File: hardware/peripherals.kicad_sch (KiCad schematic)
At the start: 32 parts, among them J6 Conn_01x02, J7 USB_C_Receptacle_USB2.0_14P, J8 Conn_01x03, Q4 2N7002, SW1 SW_Push, U3 74AHCT1G125, U4 DS3231MZ, U5 USBLC6-2SC6, U6 74AHCT1G32

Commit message: Right-angle button (Alps SKRTLAE010), adjust connector Y positions, add 3D models
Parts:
- SW1: footprint Button_Switch_SMD:SW_Push_1TS009xxxx-xxxx-xxxx_6x6x5mm -> Button_Switch_SMD:SW_Push_1P1T-MP_NO_Horizontal_Alps_SKRTLAE010
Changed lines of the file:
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@@
 			)
 		)
-		(property "Footprint" "Button_Switch_SMD:SW_Push_1TS009xxxx-xxxx-xxxx_6x6x5mm"
+		(property "Footprint" "Button_Switch_SMD:SW_Push_1P1T-MP_NO_Horizontal_Alps_SKRTLAE010"
 			(at 246.38 40.64 0)
 			(hide yes)

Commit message: Replace reverse-mount LED with standard 5050 SK6812 for light pipe
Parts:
- D1: footprint LED_SMD:LED_SK6812MINI-E_3.2x2.8mm_P1.5mm_ReverseMount -> LED_SMD:LED_SK6812_PLCC4_5.0x5.0mm_P3.2mm
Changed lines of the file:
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@@
 			)
 		)
-		(property "Footprint" "LED_SMD:LED_SK6812MINI-E_3.2x2.8mm_P1.5mm_ReverseMount"
+		(property "Footprint" "LED_SMD:LED_SK6812_PLCC4_5.0x5.0mm_P3.2mm"
 			(at 128.27 46.99 0)
 			(hide yes)

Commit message: Fix ERC: update SK6812 symbol to match library
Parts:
- D1: footprint LED_SMD:LED_SK6812_PLCC4_5.0x5.0mm_P3.2mm -> LED_SMD:LED_SK6812MINI-E_3.2x2.8mm_P1.5mm_ReverseMount
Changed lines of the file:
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@@
 			)
 		)
-		(property "Footprint" "LED_SMD:LED_SK6812_PLCC4_5.0x5.0mm_P3.2mm"
+		(property "Footprint" "LED_SMD:LED_SK6812MINI-E_3.2x2.8mm_P1.5mm_ReverseMount"
 			(at 128.27 46.99 0)
 			(hide yes)

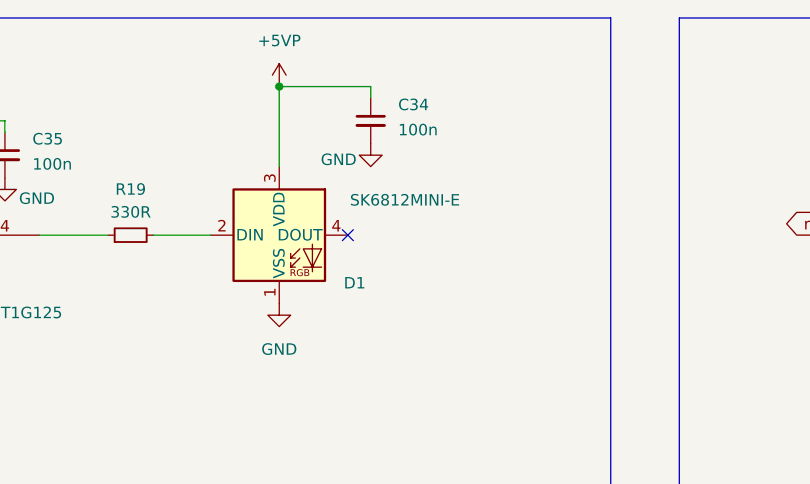
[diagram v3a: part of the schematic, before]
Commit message: Change NeoPixel D1 to WS2812B 5mm SMD (PLCC4)
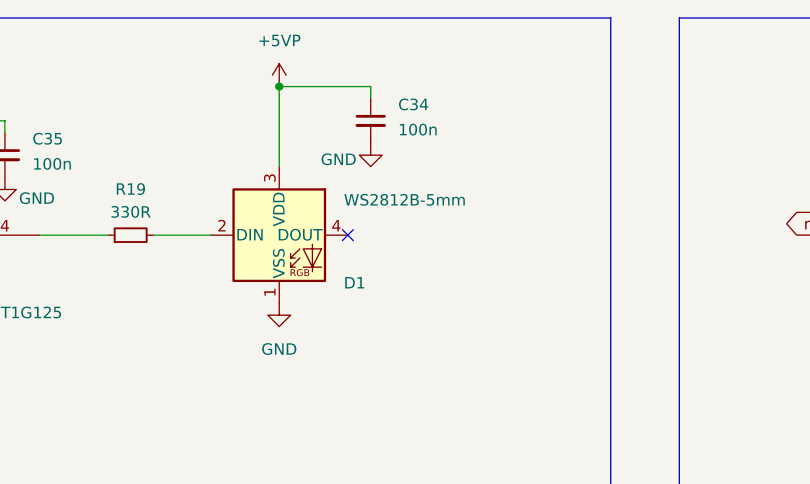
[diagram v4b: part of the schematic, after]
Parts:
- D1: value SK6812MINI-E -> WS2812B-5mm; footprint LED_SMD:LED_SK6812MINI-E_3.2x2.8mm_P1.5mm_ReverseMount -> LED_SMD:LED_WS2812B_PLCC4_5.0x5.0mm_P3.2mm
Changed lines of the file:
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@@
 			)
 		)
-		(property "Value" "SK6812MINI-E"
+		(property "Value" "WS2812B-5mm"
 			(at 140.97 35.4898 0)
 			(show_name no)
@@
 			)
 		)
-		(property "Footprint" "LED_SMD:LED_SK6812MINI-E_3.2x2.8mm_P1.5mm_ReverseMount"
+		(property "Footprint" "LED_SMD:LED_WS2812B_PLCC4_5.0x5.0mm_P3.2mm"
 			(at 128.27 46.99 0)
 			(hide yes)

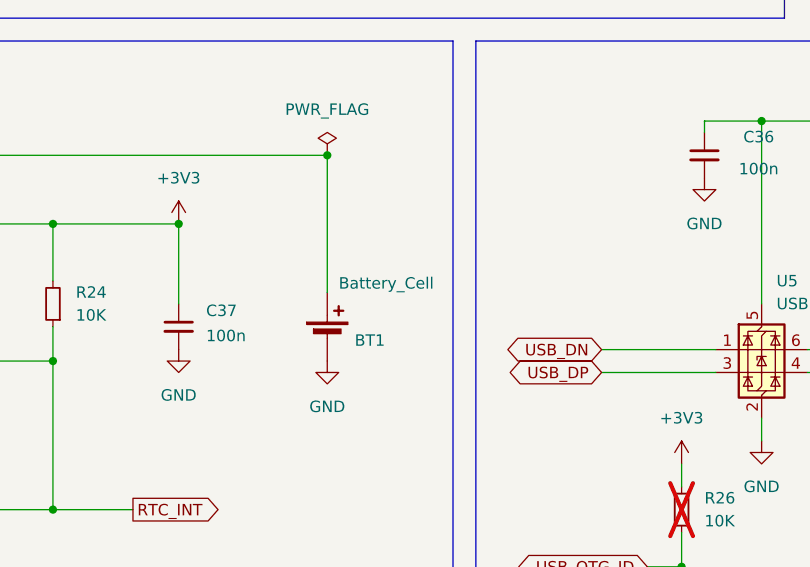
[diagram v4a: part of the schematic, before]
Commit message: fix: add missing BOM values for F1 (3A), Y1 (25MHz), BT1 (CR2032)
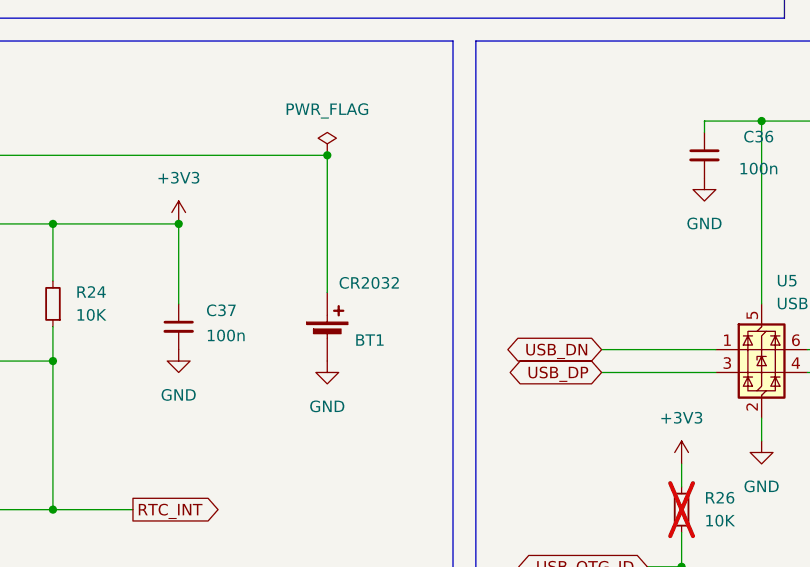
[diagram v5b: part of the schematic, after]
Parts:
- BT1: value Battery_Cell -> CR2032
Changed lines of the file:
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@@
 			)
 		)
-		(property "Value" "Battery_Cell"
+		(property "Value" "CR2032"
 			(at 114.3 99.314 0)
 			(show_name no)

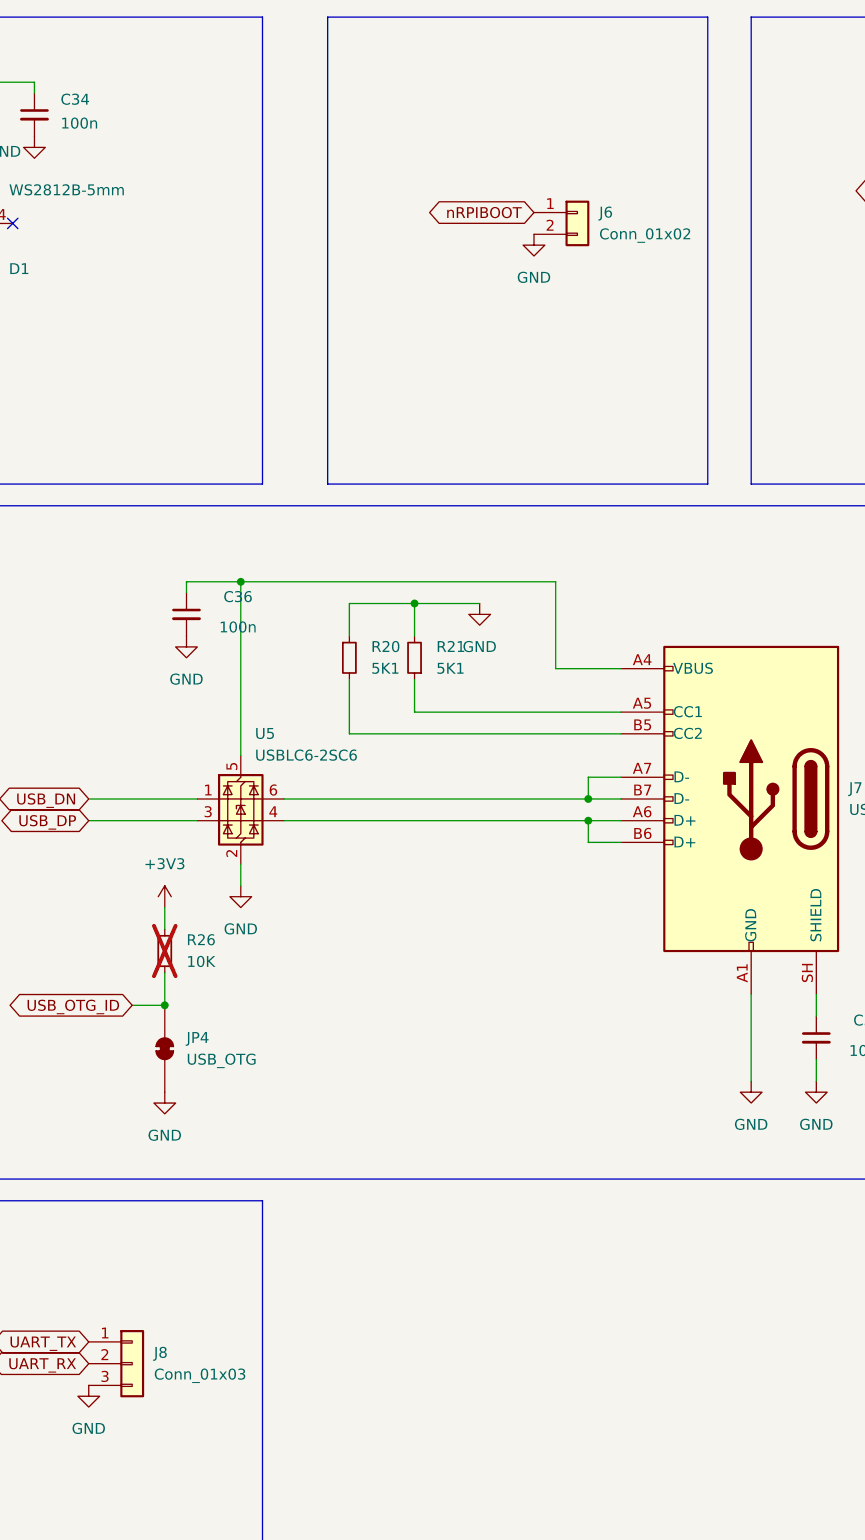
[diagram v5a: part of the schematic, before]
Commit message: feat: replace J6 with PCM12SMTR slide switch, J8 with JST-SH 3-pin
J6 (nRPIBOOT): pin header + jumper → SPDT slide switch (SW_SPDT_312)
J8 (UART debug): 2.54mm pin header → JST-SH SM03B-SRSS-TB (latching)
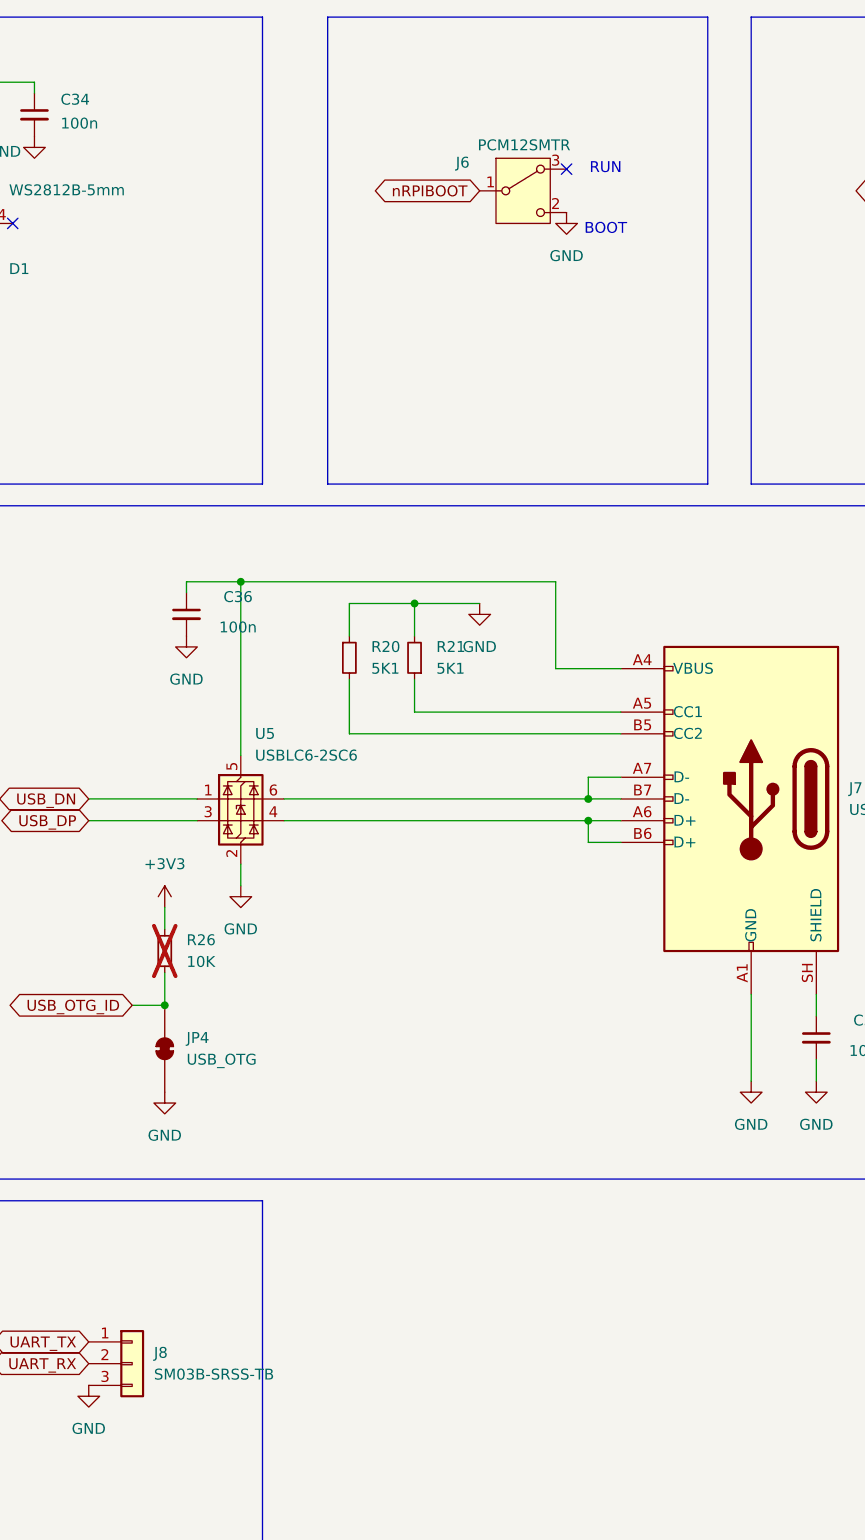
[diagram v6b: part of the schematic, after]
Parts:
- J6: value Conn_01x02 -> PCM12SMTR; footprint Connector_PinHeader_2.54mm:PinHeader_1x02_P2.54mm_Vertical -> Button_Switch_SMD:SW_SPDT_PCM12; symbol Connector_Generic:Conn_01x02 -> Switch:SW_SPDT_312
- J8: value Conn_01x03 -> SM03B-SRSS-TB; footprint Connector_PinHeader_2.54mm:PinHeader_1x03_P2.54mm_Vertical -> Connector_JST:JST_SH_SM03B-SRSS-TB_1x03-1MP_P1.00mm_Horizontal
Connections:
- no-connect marks 2 -> 3
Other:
- note added: "BOOT"
- note added: "RUN"
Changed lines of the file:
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@@
 		)
 	)
+	(text "BOOT"
+		(exclude_from_sim no)
+		(at 203.962 40.132 0)
+		(effects
+			(font
+				(size 1.27 1.27)
+			)
+		)
+	)
+	(text "RUN"
+		(exclude_from_sim no)
+		(at 203.962 33.02 0)
+		(effects
+			(font
+				(size 1.27 1.27)
+			)
+		)
+	)
 	(junction
 		(at 55.88 146.05)
@@
 	)
 	(no_connect
+		(at 199.39 33.02)
+	)
+	(no_connect
 		(at 74.93 100.33)
 	)
@@
 	(global_label "nRPIBOOT"
 		(shape bidirectional)
-		(at 195.58 38.1 180)
+		(at 189.23 35.56 180)
 		(fields_autoplaced yes)
 		(effects
@@
 		)
 		(property "Intersheetrefs" "${INTERSHEET_REFS}"
-			(at 182.2911 38.1 0)
+			(at 175.9411 35.56 0)
 			(hide yes)
 			(show_name no)
@@
 	(symbol
 		(lib_id "power:GND")
-		(at 195.58 40.64 0)
+		(at 199.39 38.1 0)
 		(unit 1)
 		(body_style 1)
@@
 		(fields_autoplaced yes)
 		(property "Reference" "#PWR056"
-			(at 195.58 46.99 0)
+			(at 199.39 44.45 0)
 			(hide yes)
 			(show_name no)
@@
 		)
 		(property "Value" "GND"
-			(at 195.58 45.72 0)
+			(at 199.39 43.18 0)
 			(show_name no)
 			(do_not_autoplace no)
@@
 		)
 		(property "Footprint" ""
-			(at 195.58 40.64 0)
+			(at 199.39 38.1 0)
 			(hide yes)
 			(show_name no)
@@
 		)
 		(property "Datasheet" ""
-			(at 195.58 40.64 0)
+			(at 199.39 38.1 0)
 			(hide yes)
 			(show_name no)
@@
 		)
 		(property "Description" "Power symbol creates a global label with name \"GND\" , ground"
-			(at 195.58 40.64 0)
+			(at 199.39 38.1 0)
 			(hide yes)
 			(show_name no)
@@
 	)
 	(symbol
-		(lib_id "Connector_Generic:Conn_01x02")
-		(at 200.66 38.1 0)
+		(lib_id "Switch:SW_SPDT_312")
+		(at 194.31 35.56 0)
 		(unit 1)
 		(body_style 1)
@@
 		(in_pos_files yes)
 		(dnp no)
-		(fields_autoplaced yes)
 		(property "Reference" "J6"
-			(at 203.2 38.0999 0)
+			(at 186.436 32.258 0)
 			(show_name no)
 			(do_not_autoplace no)
@@
 			)
 		)
-		(property "Value" "Conn_01x02"
-			(at 203.2 40.6399 0)
+		(property "Value" "PCM12SMTR"
+			(at 188.976 30.226 0)
 			(show_name no)
 			(do_not_autoplace no)
@@
 			)
 		)
-		(property "Footprint" "Connector_PinHeader_2.54mm:PinHeader_1x02_P2.54mm_Vertical"
-			(at 200.66 38.1 0)
+		(property "Footprint" "Button_Switch_SMD:SW_SPDT_PCM12"
+			(at 194.31 35.56 0)
 			(hide yes)
 			(show_name no)
@@
 		)
 		(property "Datasheet" ""
-			(at 200.66 38.1 0)
+			(at 194.31 35.56 0)
 			(hide yes)
 			(show_name no)
@@
 			)
 		)
-		(property "Description" "Generic connector, single row, 01x02, script generated (kicad-library-utils/schlib/autogen/connector/)"
-			(at 200.66 38.1 0)
+		(property "Description" "Switch, single pole double throw"
+			(at 194.31 35.56 0)
 			(hide yes)
 			(show_name no)
@@
 		(pin "1"
 		)
+		(pin "3"
+		)
 		(instances
 			(project "granit"
@@
 			)
 		)
-		(property "Value" "Conn_01x03"
+		(property "Value" "SM03B-SRSS-TB"
 			(at 151.13 173.9899 0)
 			(show_name no)
@@
 			)
 		)
-		(property "Footprint" "Connector_PinHeader_2.54mm:PinHeader_1x03_P2.54mm_Vertical"
+		(property "Footprint" "Connector_JST:JST_SH_SM03B-SRSS-TB_1x03-1MP_P1.00mm_Horizontal"
 			(at 148.59 172.72 0)
 			(hide yes)

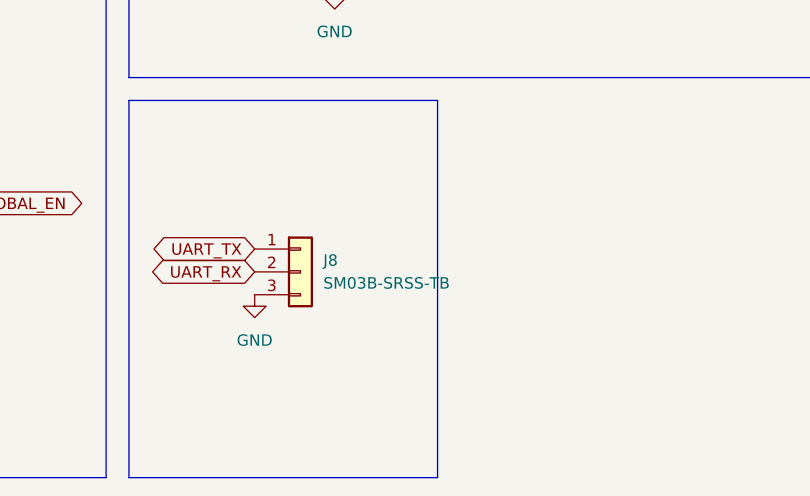
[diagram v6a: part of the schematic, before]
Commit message: fix: J8 use vertical JST-SH (BM03B-SRSS-TB)
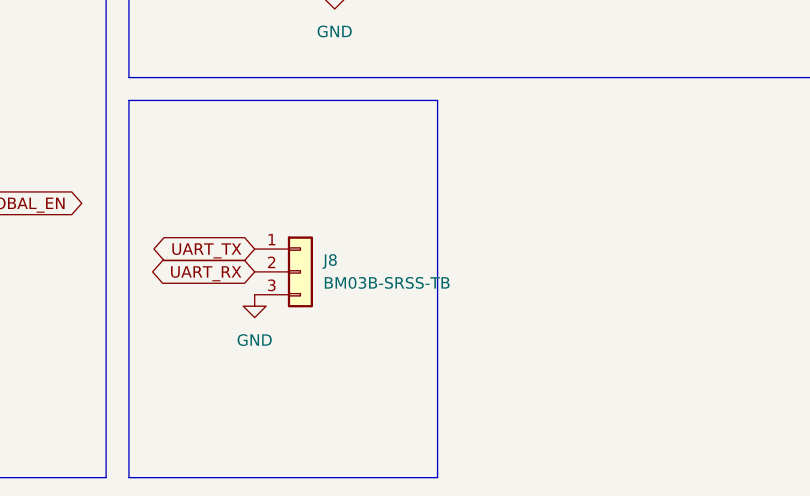
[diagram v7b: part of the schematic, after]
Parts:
- J8: value SM03B-SRSS-TB -> BM03B-SRSS-TB; footprint Connector_JST:JST_SH_SM03B-SRSS-TB_1x03-1MP_P1.00mm_Horizontal -> Connector_JST:JST_SH_BM03B-SRSS-TB_1x03-1MP_P1.00mm_Vertical
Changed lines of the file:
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@@
 			)
 		)
-		(property "Value" "SM03B-SRSS-TB"
+		(property "Value" "BM03B-SRSS-TB"
 			(at 151.13 173.9899 0)
 			(show_name no)
@@
 			)
 		)
-		(property "Footprint" "Connector_JST:JST_SH_SM03B-SRSS-TB_1x03-1MP_P1.00mm_Horizontal"
+		(property "Footprint" "Connector_JST:JST_SH_BM03B-SRSS-TB_1x03-1MP_P1.00mm_Vertical"
 			(at 148.59 172.72 0)
 			(hide yes)

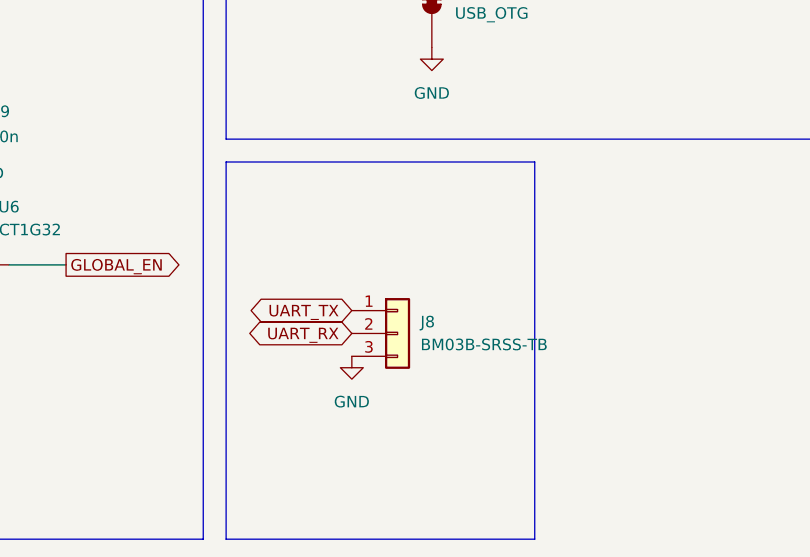
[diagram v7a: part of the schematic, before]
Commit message: fix: J6/J8 wiring and PCB layout after connector swap
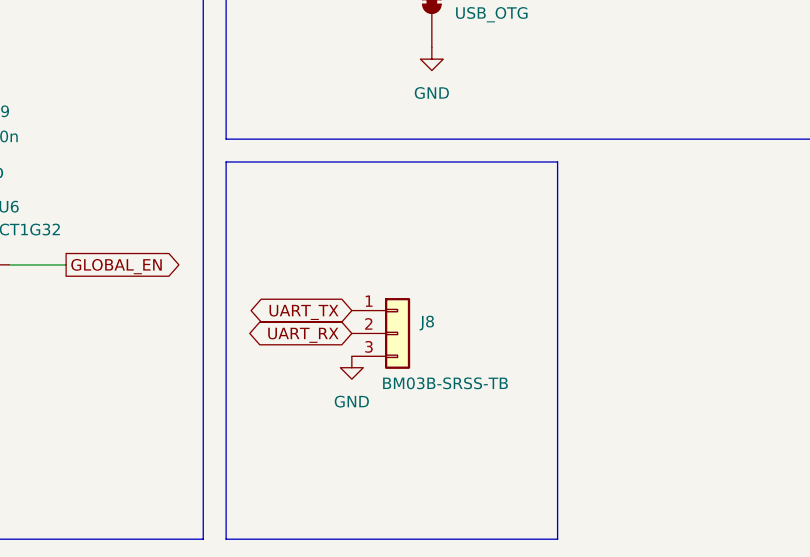
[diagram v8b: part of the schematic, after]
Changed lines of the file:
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@@
 	(rectangle
 		(start 129.54 153.67)
-		(end 163.83 195.58)
+		(end 166.37 195.58)
 		(stroke
 			(width 0)
@@
 		(in_pos_files yes)
 		(dnp no)
-		(fields_autoplaced yes)
 		(property "Reference" "J8"
 			(at 151.13 171.4499 0)
@@
 		)
 		(property "Value" "BM03B-SRSS-TB"
-			(at 151.13 173.9899 0)
+			(at 146.812 178.308 0)
 			(show_name no)
 			(do_not_autoplace no)
